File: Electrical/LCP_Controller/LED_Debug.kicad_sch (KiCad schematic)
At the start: 13 parts

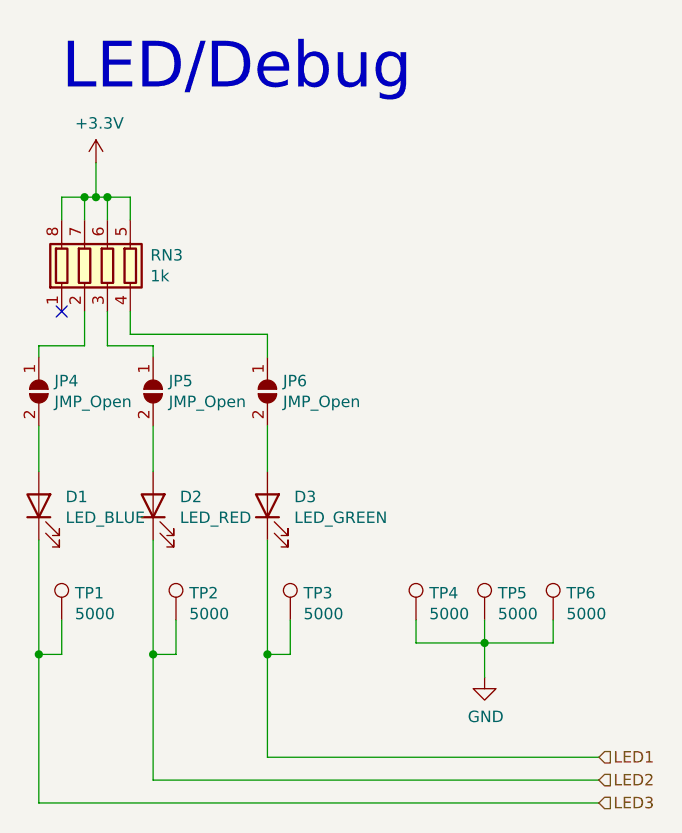
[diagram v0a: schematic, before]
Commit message: Hardware Revision : v0.3
1. modified schematic design, removed unnecessary test points.
2. pcb layout 2x8 Inches allowance dimension, layout is in progress
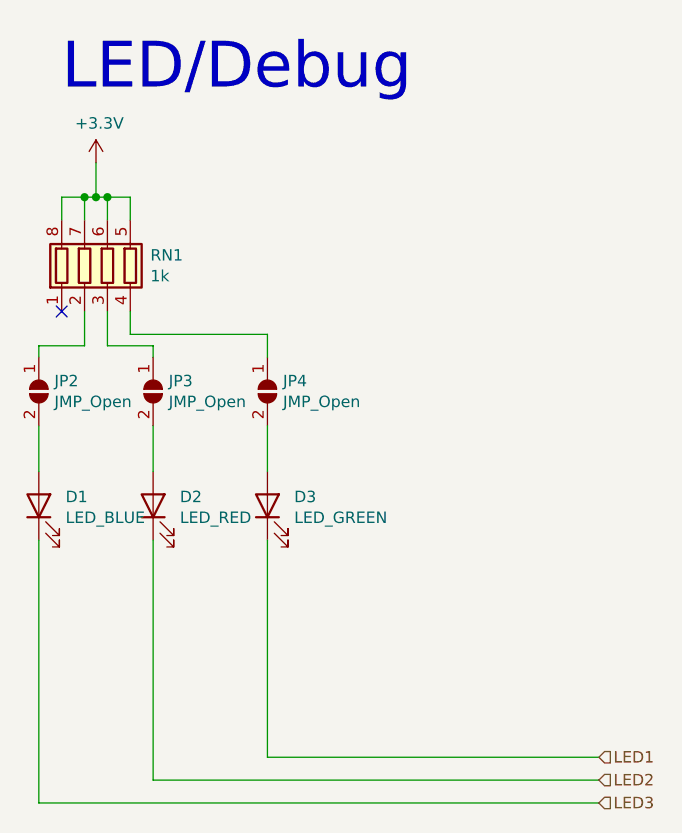
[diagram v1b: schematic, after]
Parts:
- removed TP1, TP2, TP3, TP4, TP5, TP6: 5000, TestPoint:TestPoint_Keystone_5000-5004_Miniature, symbol Connector:TestPoint
- renumbered JP4 to JP2, JP5 to JP3, JP6 to JP4, RN3 to RN1

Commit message: Removed RF Switch
Deleted the RF Switch.

GPS Signal is routed to J17 and Iridium to J18.
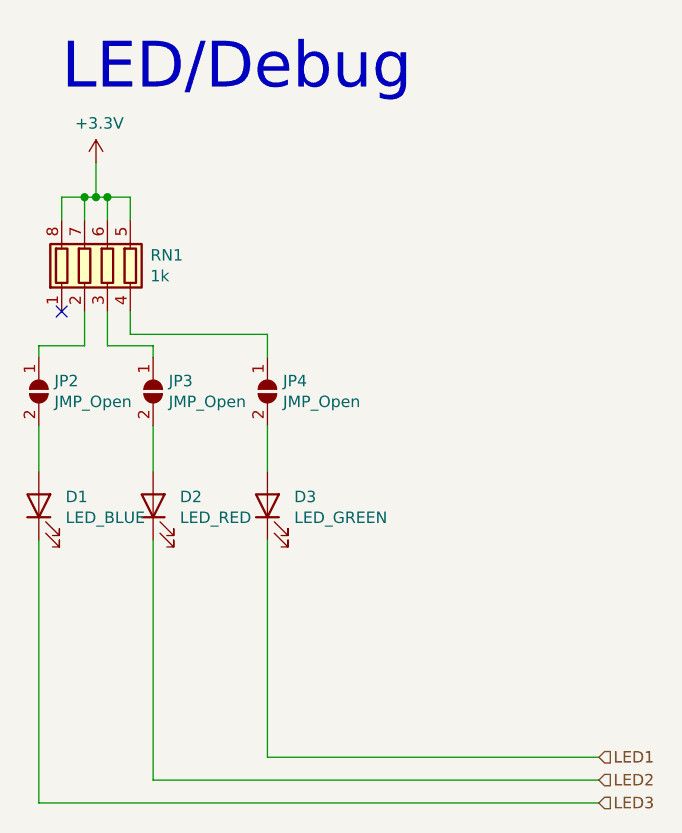
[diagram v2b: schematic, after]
